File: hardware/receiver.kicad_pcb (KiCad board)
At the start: 2 copper layers, 71.8 x 43.7 mm, 94 parts, among them J1 Conn_01x05_Male, J2 USB-C, J3 Left, J4 Right, Q1 S8050, Q2 S8050, Q3 AO3400A, Q4 AO3401A, SW1 Enable, SW2 Boot, U1 SN65HVD230, U2 CH340C, U3 AMS1117-3.3, U4 ESP32-WROOM-32E, U5 TP6841S6-A, U6 AMS1117-3.3, U7 AMS1117-3.3, U8 PCM5102A

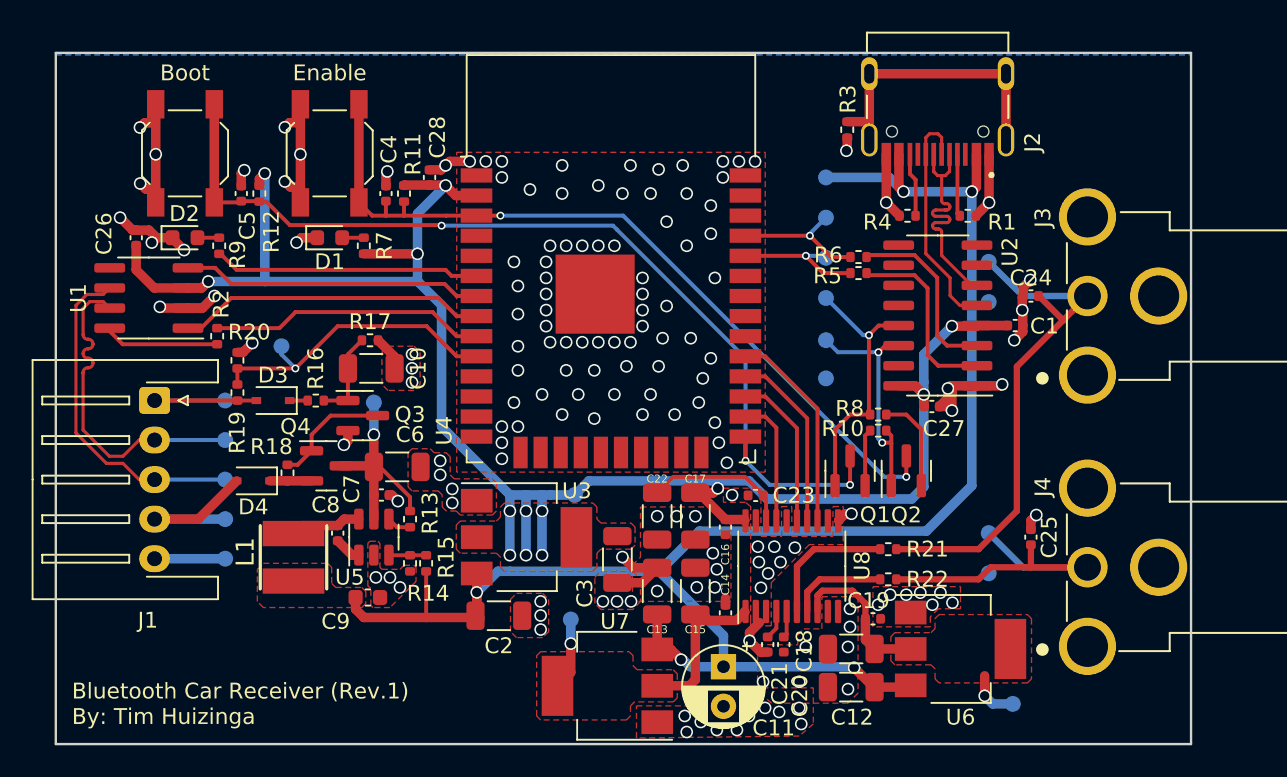
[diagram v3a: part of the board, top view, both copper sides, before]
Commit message: Made corners rounded and added mounting holes
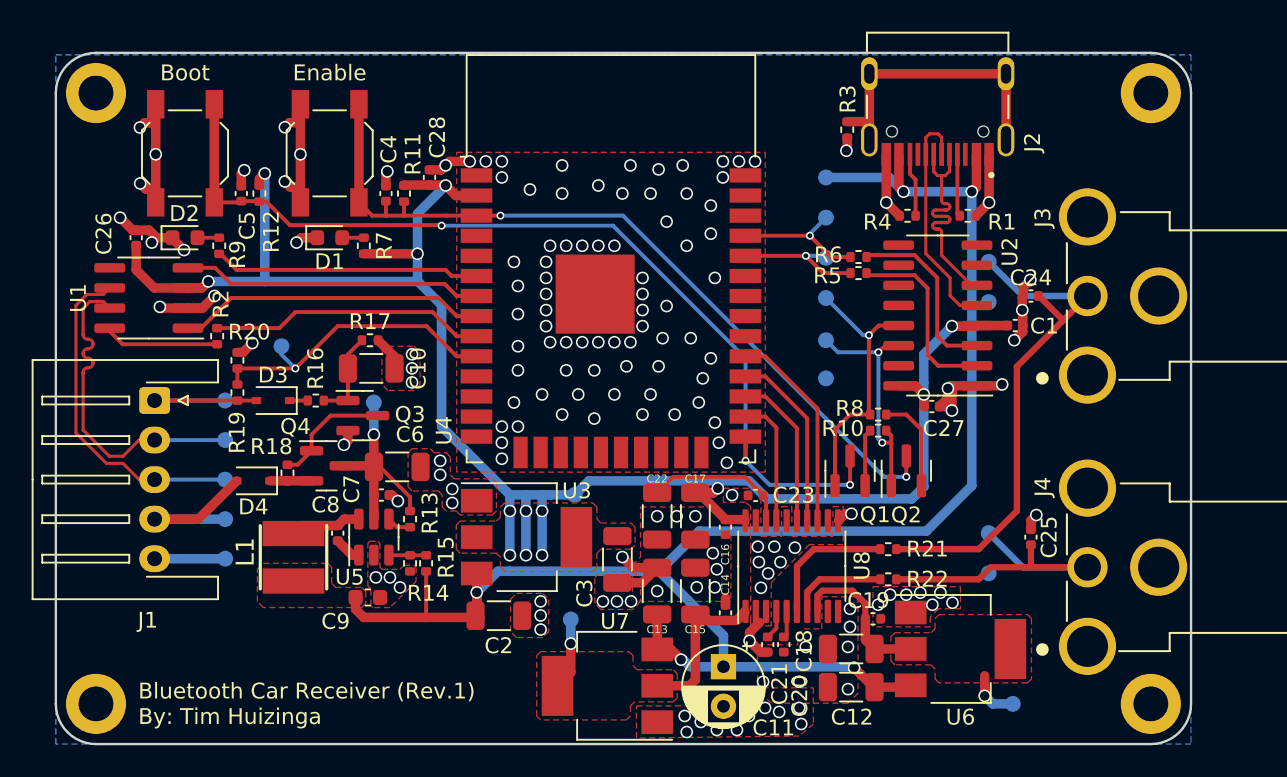
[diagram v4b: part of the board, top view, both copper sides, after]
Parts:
- added H1: M2, MountingHole:MountingHole_2.2mm_M2_ISO14580_Pad, F.Cu at (53.0, 108.2)
- added H2: M2, MountingHole:MountingHole_2.2mm_M2_ISO14580_Pad, F.Cu at (119.7, 108.2)
- added H3: M2, MountingHole:MountingHole_2.2mm_M2_ISO14580_Pad, F.Cu at (119.7, 146.8)
- added H4: M2, MountingHole:MountingHole_2.2mm_M2_ISO14580_Pad, F.Cu at (53.0, 146.8)
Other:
- outline, holes or cut-outs redrawn
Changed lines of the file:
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@@
     )
   )
+  (footprint "MountingHole:MountingHole_2.2mm_M2_ISO14580_Pad" (layer "F.Cu")
+    (at 53.048 108.204)
+    (descr "Mounting Hole 2.2mm, M2, ISO14580")
+    (tags "mounting hole 2.2mm m2 iso14580")
+    (property "Sheetfile" "receiver.kicad_sch")
+    (property "Sheetname" "")
+    (attr exclude_from_pos_files)
+    (fp_text reference "H1" (at 0 -2.9) (layer "F.SilkS") hide
+      (effects (font (size 1 1) (thickness 0.15)))
+    )
+    (fp_text value "M2" (at 0 2.9) (layer "F.Fab")
+      (effects (font (size 1 1) (thickness 0.15)))
+    )
+    (fp_text user "${REFERENCE}" (at 0 0) (layer "F.Fab")
+      (effects (font (size 1 1) (thickness 0.15)))
+    )
+    (fp_circle (center 0 0) (end 1.9 0) (layer "Cmts.User") (width 0.15) (fill none))
+    (fp_circle (center 0 0) (end 2.15 0) (layer "F.CrtYd") (width 0.05) (fill none))
+    (pad "1" thru_hole circle (at 0 0) (size 3.8 3.8) (drill 2.2) (layers *.Cu *.Mask)
+      (net 2 "GND") (pinfunction "1") (pintype "input"))
+  )
   (footprint "Package_TO_SOT_SMD:SOT-223-3_TabPin2" (layer "F.Cu")
     (at 85.369 145.669 180)
@@
     )
   )
+  (footprint "MountingHole:MountingHole_2.2mm_M2_ISO14580_Pad" (layer "F.Cu")
+    (at 119.723 108.204)
+    (descr "Mounting Hole 2.2mm, M2, ISO14580")
+    (tags "mounting hole 2.2mm m2 iso14580")
+    (property "Sheetfile" "receiver.kicad_sch")
+    (property "Sheetname" "")
+    (attr exclude_from_pos_files)
+    (fp_text reference "H2" (at 0 -2.9) (layer "F.SilkS") hide
+      (effects (font (size 1 1) (thickness 0.15)))
+    )
+    (fp_text value "M2" (at 0 2.9) (layer "F.Fab")
+      (effects (font (size 1 1) (thickness 0.15)))
+    )
+    (fp_text user "${REFERENCE}" (at 0 0) (layer "F.Fab")
+      (effects (font (size 1 1) (thickness 0.15)))
+    )
+    (fp_circle (center 0 0) (end 1.9 0) (layer "Cmts.User") (width 0.15) (fill none))
+    (fp_circle (center 0 0) (end 2.15 0) (layer "F.CrtYd") (width 0.05) (fill none))
+    (pad "1" thru_hole circle (at 0 0) (size 3.8 3.8) (drill 2.2) (layers *.Cu *.Mask)
+      (net 2 "GND") (pinfunction "1") (pintype "input"))
+  )
   (footprint "Capacitor_SMD:C_0402_1005Metric" (layer "F.Cu")
     (at 68.326 136.0225 90)
@@
     )
   )
+  (footprint "MountingHole:MountingHole_2.2mm_M2_ISO14580_Pad" (layer "F.Cu")
+    (at 119.723 146.812)
+    (descr "Mounting Hole 2.2mm, M2, ISO14580")
+    (tags "mounting hole 2.2mm m2 iso14580")
+    (property "Sheetfile" "receiver.kicad_sch")
+    (property "Sheetname" "")
+    (attr exclude_from_pos_files)
+    (fp_text reference "H3" (at 0 -2.9) (layer "F.SilkS") hide
+      (effects (font (size 1 1) (thickness 0.15)))
+    )
+    (fp_text value "M2" (at 0 2.9) (layer "F.Fab")
+      (effects (font (size 1 1) (thickness 0.15)))
+    )
+    (fp_text user "${REFERENCE}" (at 0 0) (layer "F.Fab")
+      (effects (font (size 1 1) (thickness 0.15)))
+    )
+    (fp_circle (center 0 0) (end 1.9 0) (layer "Cmts.User") (width 0.15) (fill none))
+    (fp_circle (center 0 0) (end 2.15 0) (layer "F.CrtYd") (width 0.05) (fill none))
+    (pad "1" thru_hole circle (at 0 0) (size 3.8 3.8) (drill 2.2) (layers *.Cu *.Mask)
+      (net 2 "GND") (pinfunction "1") (pintype "input"))
+  )
   (footprint "Resistor_SMD:R_0402_1005Metric" (layer "F.Cu")
     (at 61.987 125.1 90)
@@
     )
   )
+  (footprint "MountingHole:MountingHole_2.2mm_M2_ISO14580_Pad" (layer "F.Cu")
+    (at 53.048 146.812)
+    (descr "Mounting Hole 2.2mm, M2, ISO14580")
+    (tags "mounting hole 2.2mm m2 iso14580")
+    (property "Sheetfile" "receiver.kicad_sch")
+    (property "Sheetname" "")
+    (attr exclude_from_pos_files)
+    (fp_text reference "H4" (at 0 -2.9) (layer "F.SilkS") hide
+      (effects (font (size 1 1) (thickness 0.15)))
+    )
+    (fp_text value "M2" (at 0 2.9) (layer "F.Fab")
+      (effects (font (size 1 1) (thickness 0.15)))
+    )
+    (fp_text user "${REFERENCE}" (at 0 0) (layer "F.Fab")
+      (effects (font (size 1 1) (thickness 0.15)))
+    )
+    (fp_circle (center 0 0) (end 1.9 0) (layer "Cmts.User") (width 0.15) (fill none))
+    (fp_circle (center 0 0) (end 2.15 0) (layer "F.CrtYd") (width 0.05) (fill none))
+    (pad "1" thru_hole circle (at 0 0) (size 3.8 3.8) (drill 2.2) (layers *.Cu *.Mask)
+      (net 2 "GND") (pinfunction "1") (pintype "input"))
+  )
   (footprint "Capacitor_SMD:C_0402_1005Metric" (layer "F.Cu")
     (at 71.374 114.554 90)
@@
       (net 2 "GND") (pinfunction "1") (pintype "passive"))
   )
-  (gr_line (start 122.263 105.664) (end 50.508 105.664) (layer "Edge.Cuts") (width 0.15))
-  (gr_line (start 122.263 149.352) (end 122.263 105.664) (layer "Edge.Cuts") (width 0.15))
-  (gr_line (start 50.508 149.352) (end 122.263 149.352) (layer "Edge.Cuts") (width 0.15))
-  (gr_line (start 50.508 105.664) (end 50.508 149.352) (layer "Edge.Cuts") (width 0.15))
-  (gr_text "Bluetooth Car Receiver (Rev.1)\nBy: Tim Huizinga" (at 51.524 146.812) (layer "F.SilkS")
+  (gr_arc (start 119.723 105.664) (mid 121.519051 106.407949) (end 122.263 108.204) (layer "Edge.Cuts") (width 0.15))
+  (gr_line (start 119.723 105.664) (end 53.048 105.664) (layer "Edge.Cuts") (width 0.15))
+  (gr_arc (start 53.048 149.352) (mid 51.251949 148.608051) (end 50.508 146.812) (layer "Edge.Cuts") (width 0.15))
+  (gr_line (start 122.263 146.812) (end 122.263 108.204) (layer "Edge.Cuts") (width 0.15))
+  (gr_line (start 53.048 149.352) (end 119.723 149.352) (layer "Edge.Cuts") (width 0.15))
+  (gr_arc (start 122.263 146.812) (mid 121.519051 148.608051) (end 119.723 149.352) (layer "Edge.Cuts") (width 0.15))
+  (gr_arc (start 50.508 108.204) (mid 51.251949 106.407949) (end 53.048 105.664) (layer "Edge.Cuts") (width 0.15))
+  (gr_line (start 50.508 108.204) (end 50.508 146.812) (layer "Edge.Cuts") (width 0.15))
+  (gr_text "Bluetooth Car Receiver (Rev.1)\nBy: Tim Huizinga" (at 55.715 146.812) (layer "F.SilkS")
     (effects (font (size 1 1) (thickness 0.15)) (justify left))
   )
